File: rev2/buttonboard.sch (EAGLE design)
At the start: 12 parts

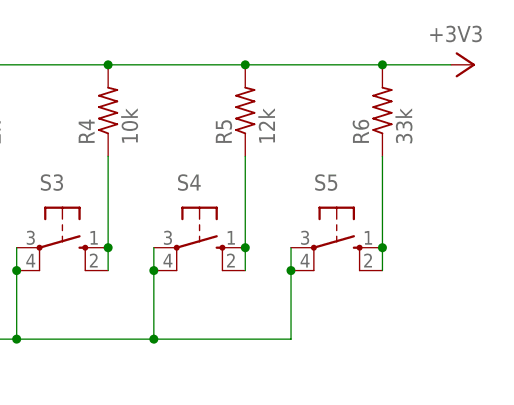
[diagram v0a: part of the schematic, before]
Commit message: Add edge connectors to lbr, Prelim PCB layout, Consolidation, Fix mistakes
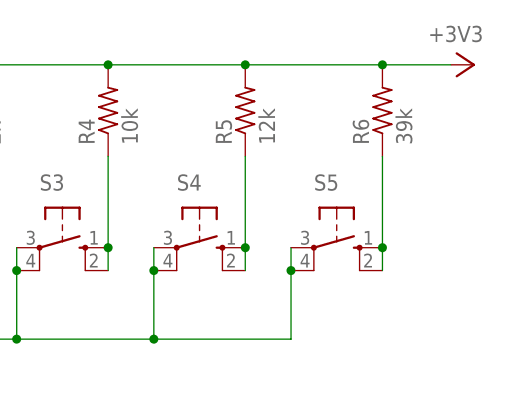
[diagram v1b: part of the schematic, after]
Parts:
- R6: value 33k -> 39k
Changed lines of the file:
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@@
 <part name="S5" library="switch-omron" library_urn="urn:adsk.eagle:library:377" deviceset="10-XX" device=""/>
 <part name="R5" library="resistor" library_urn="urn:adsk.eagle:library:348" deviceset="R-US_" device="R0805" value="12k"/>
-<part name="R6" library="resistor" library_urn="urn:adsk.eagle:library:348" deviceset="R-US_" device="R0805" value="33k"/>
+<part name="R6" library="resistor" library_urn="urn:adsk.eagle:library:348" deviceset="R-US_" device="R0805" value="39k"/>
 <part name="+3V31" library="supply1" library_urn="urn:adsk.eagle:library:371" deviceset="+3V3" device=""/>
 <part name="GND2" library="supply1" library_urn="urn:adsk.eagle:library:371" deviceset="GND" device=""/>
